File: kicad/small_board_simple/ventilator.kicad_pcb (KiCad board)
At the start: 2 copper layers, 90 x 100 mm, 36 parts, among them J1 PJ-202A, J2 Conn_01x02, J3 Conn_01x02, J5 Conn_01x02, J6 Conn_01x02, J7 Conn_01x02, J8 Conn_01x02, J9 Conn_01x02, Q3 IRLIZ44NPBF, Q4 IRLIZ44NPBF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

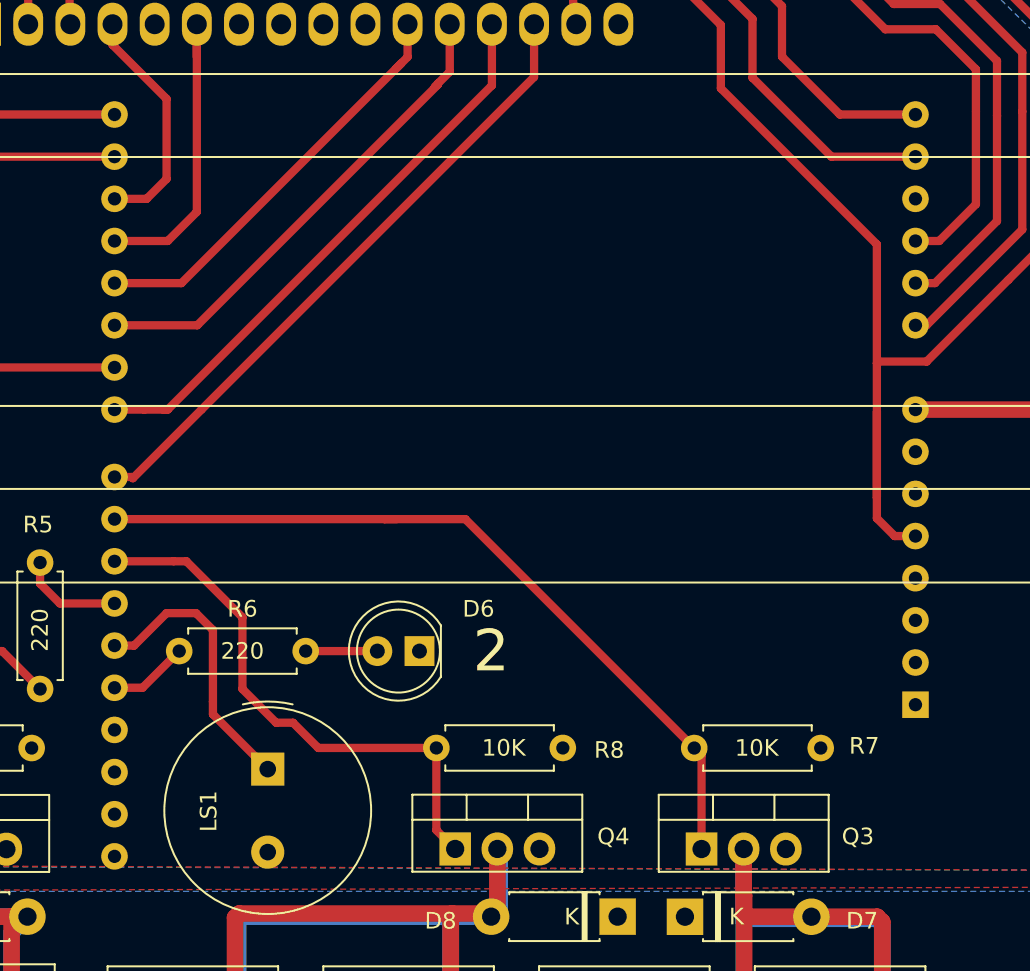
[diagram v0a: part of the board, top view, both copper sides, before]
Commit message: enlarges arduino footprint pads:
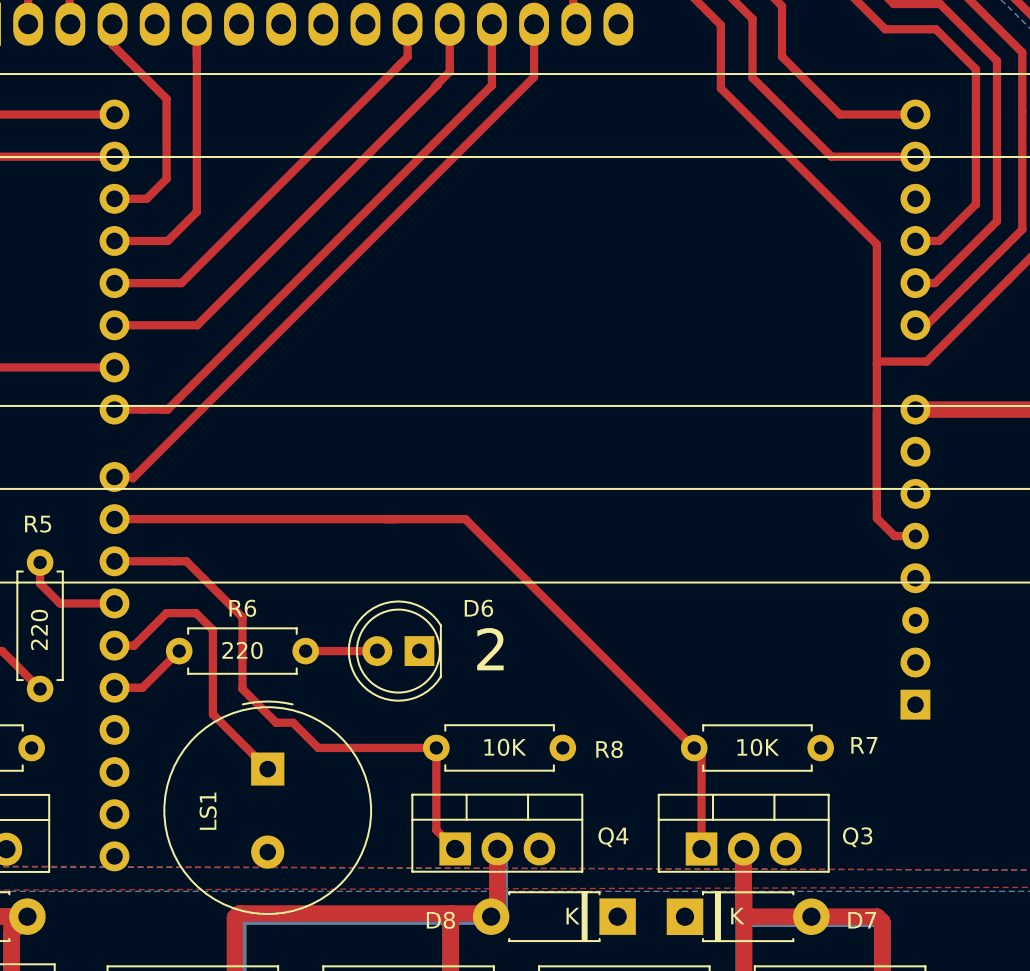
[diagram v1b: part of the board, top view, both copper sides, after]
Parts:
- A1: footprint Module:Arduino_UNO_R3 -> small_board_simple:Arduino_UNO_R3_large_pads
